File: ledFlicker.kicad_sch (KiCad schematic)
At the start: 47 parts, among them J1 Conn_01x04_Pin, J2 S2B-PH-K-SLFSN, J3 Conn_01x02_Pin, J4 USB_B_Micro, J5 Conn_01x02_Pin, Q1 BC817, U1 SPX3819M5-L, U2 MCP73831-2-OT, U4 TLC555xD, U5 TLC555xD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

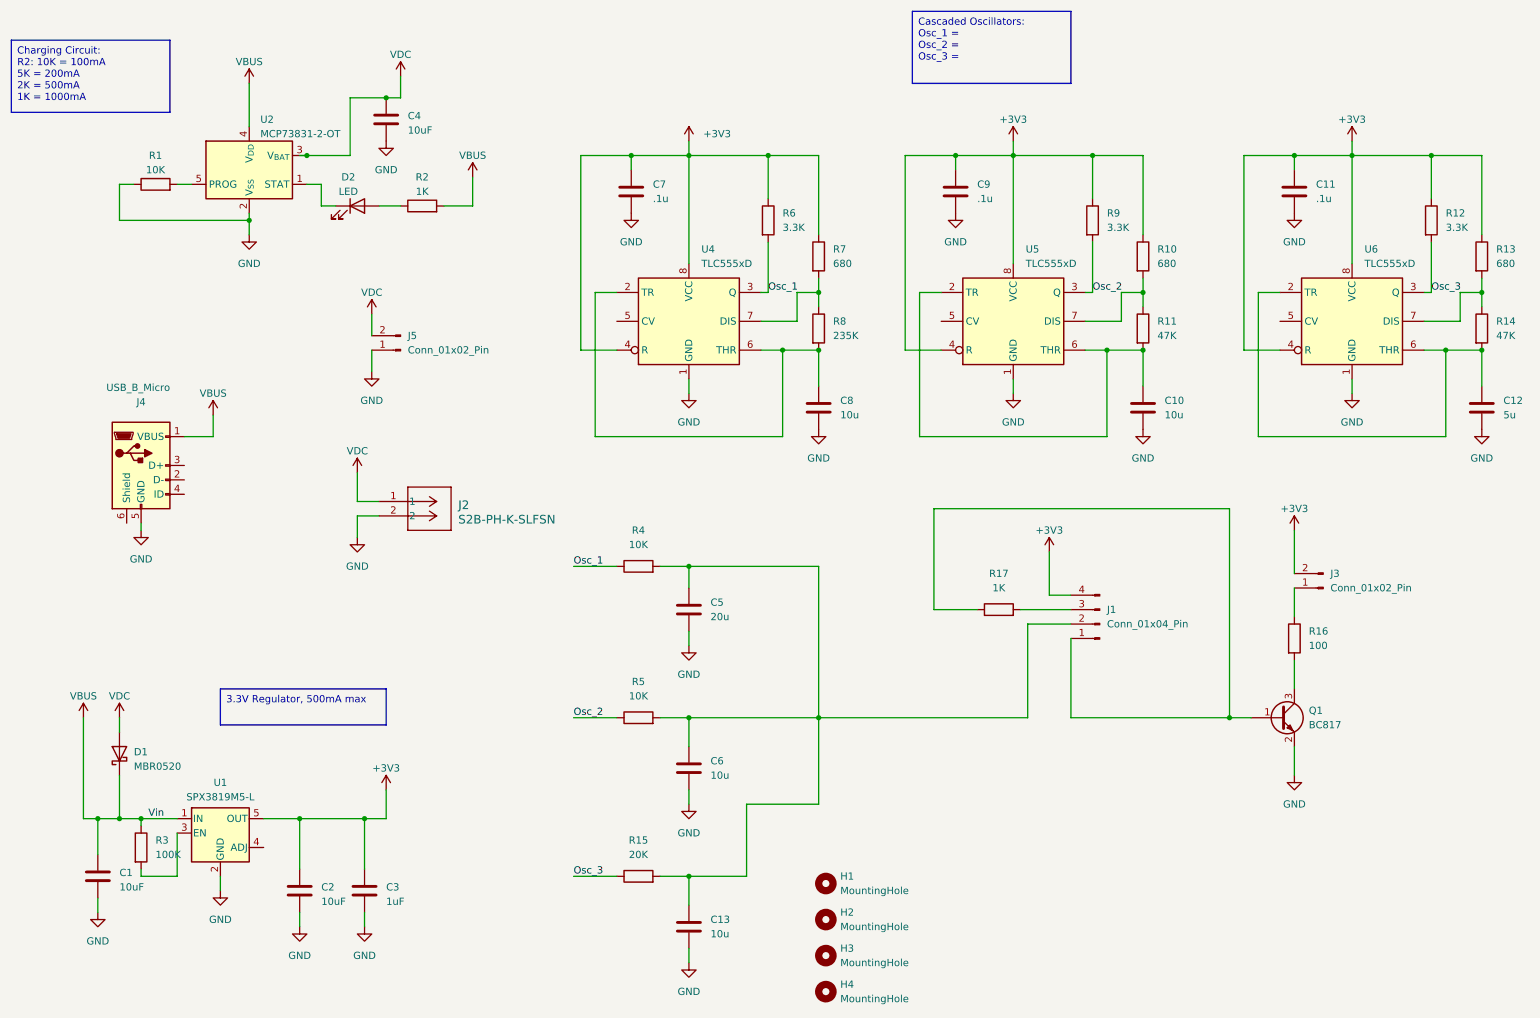
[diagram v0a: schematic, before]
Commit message: Shrunk PCB size, updated switch to OFF, FLICKER only and added R17 bias resistor
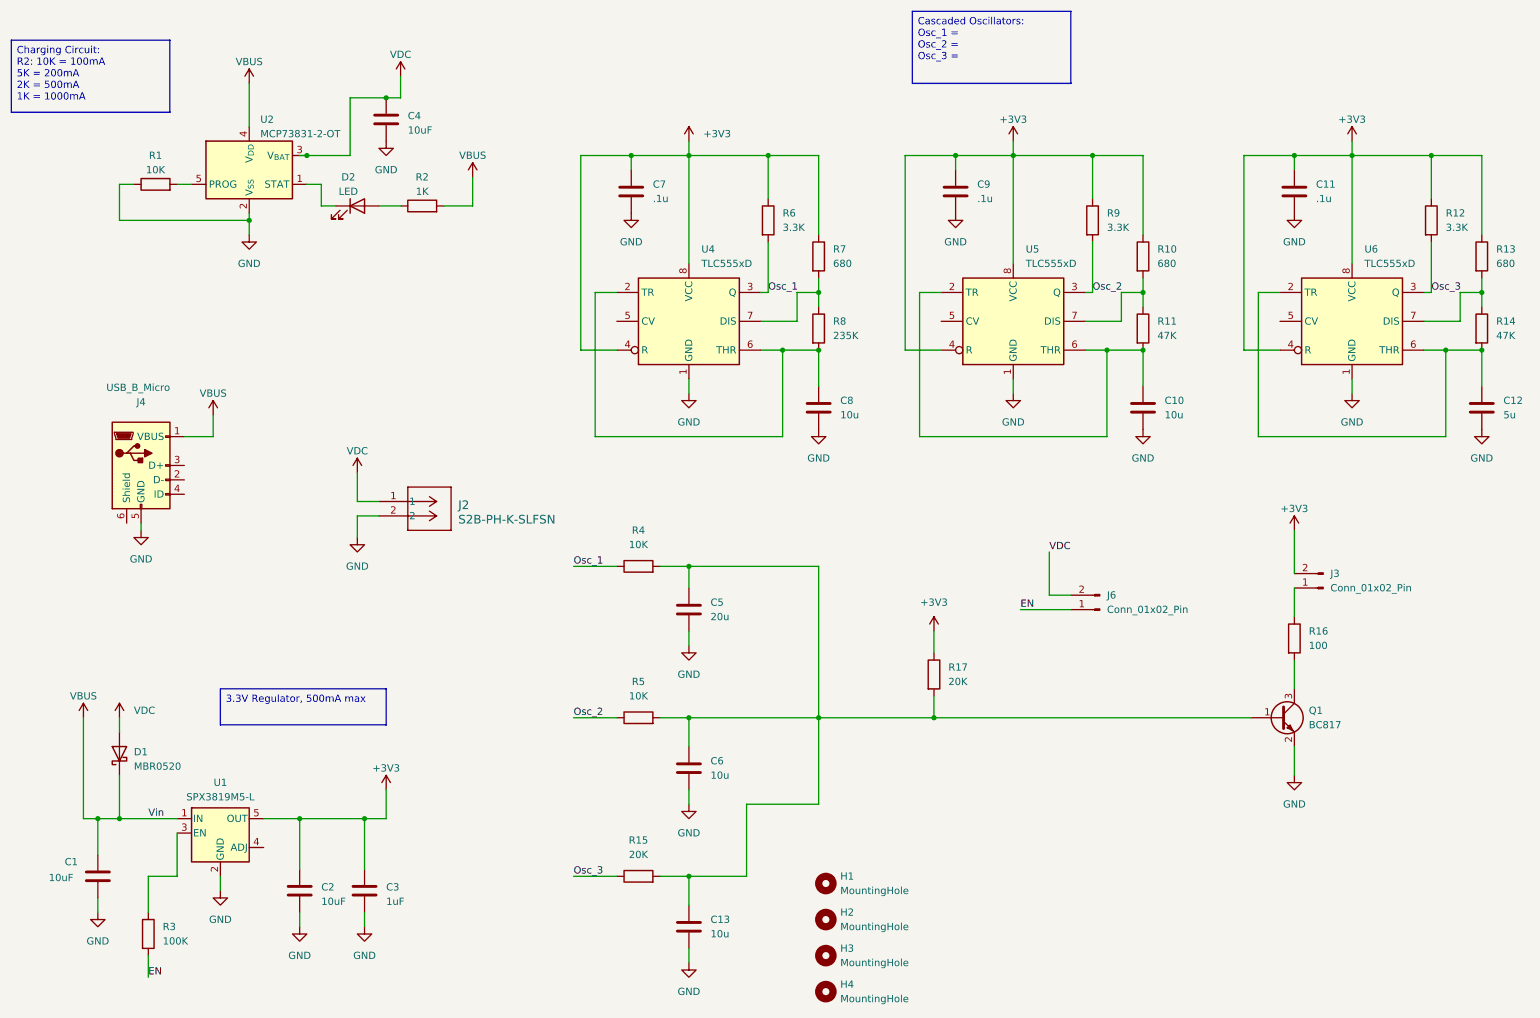
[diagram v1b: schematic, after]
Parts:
- removed J1: Conn_01x04_Pin, Connector_PinHeader_2.54mm:PinHeader_1x04_P2.54mm_Vertical, symbol Connector:Conn_01x04_Pin
- removed J5: Conn_01x02_Pin, Connector_PinHeader_2.54mm:PinHeader_1x02_P2.54mm_Vertical, symbol Connector:Conn_01x02_Pin
- added J6: Conn_01x02_Pin, Connector_PinHeader_2.54mm:PinHeader_1x02_P2.54mm_Vertical, symbol Connector:Conn_01x02_Pin
- R17: value 1K -> 20K
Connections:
- net +3V3: now also R17.1
- net VBUS: no longer R3.1
- net VDC: now also J6.2 (Pin_2)
- net at U1.3 (EN): now also R3.1; no longer R3.2
- net at C13.1, C5.1, C6.1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: now also Q1.1 (B), R17.2
- new net EN: J6.1 (Pin_1), R3.2
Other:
- moved on the sheet: R3
